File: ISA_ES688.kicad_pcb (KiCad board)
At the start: 4 copper layers, 104.1 x 99.1 mm, 114 parts, among them J1 ISA BUS, J2 Interrupt Select, J3 Address Select, J4 DMA Select, J5 Joystick/MIDI, J6 LINE OUT, J7 MIC, J8 LINE IN, J9 SPKR OUT, U1 74LS14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

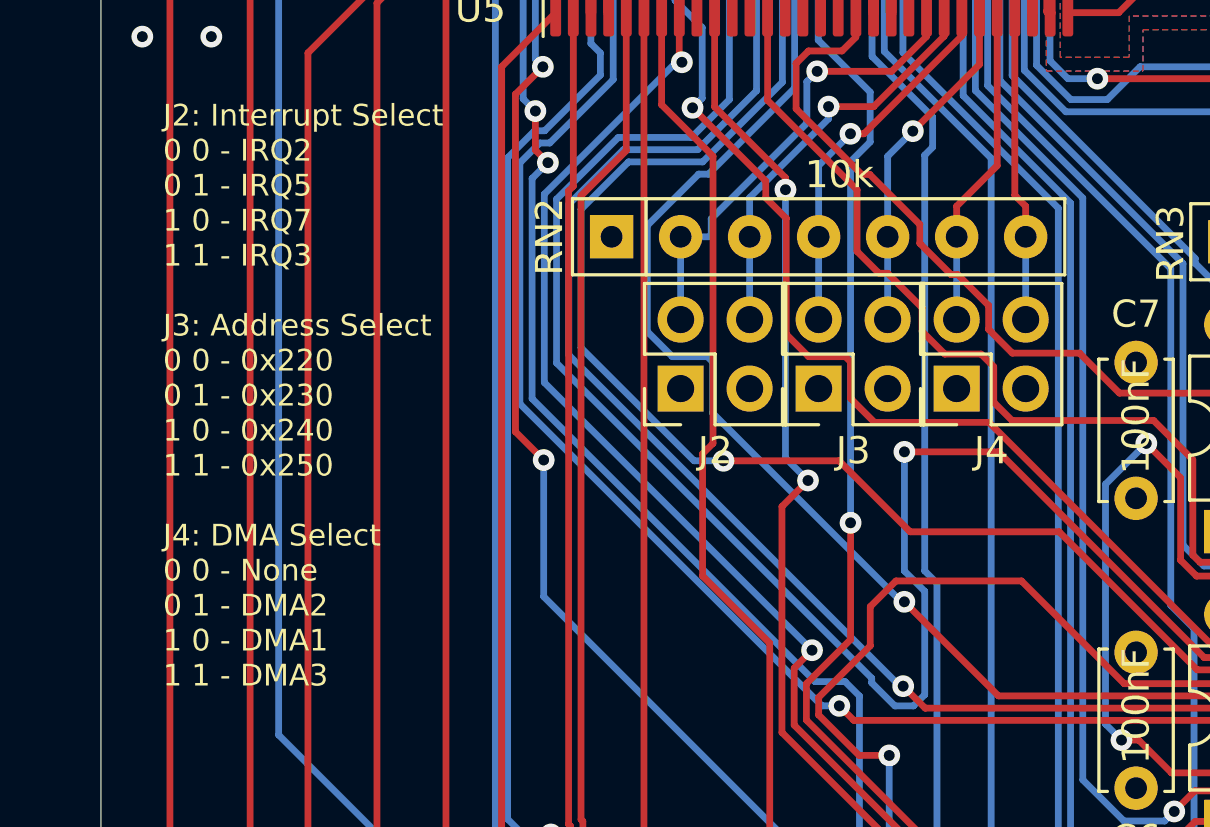
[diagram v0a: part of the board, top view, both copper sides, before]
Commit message: Updated silkscreen and version on schematic
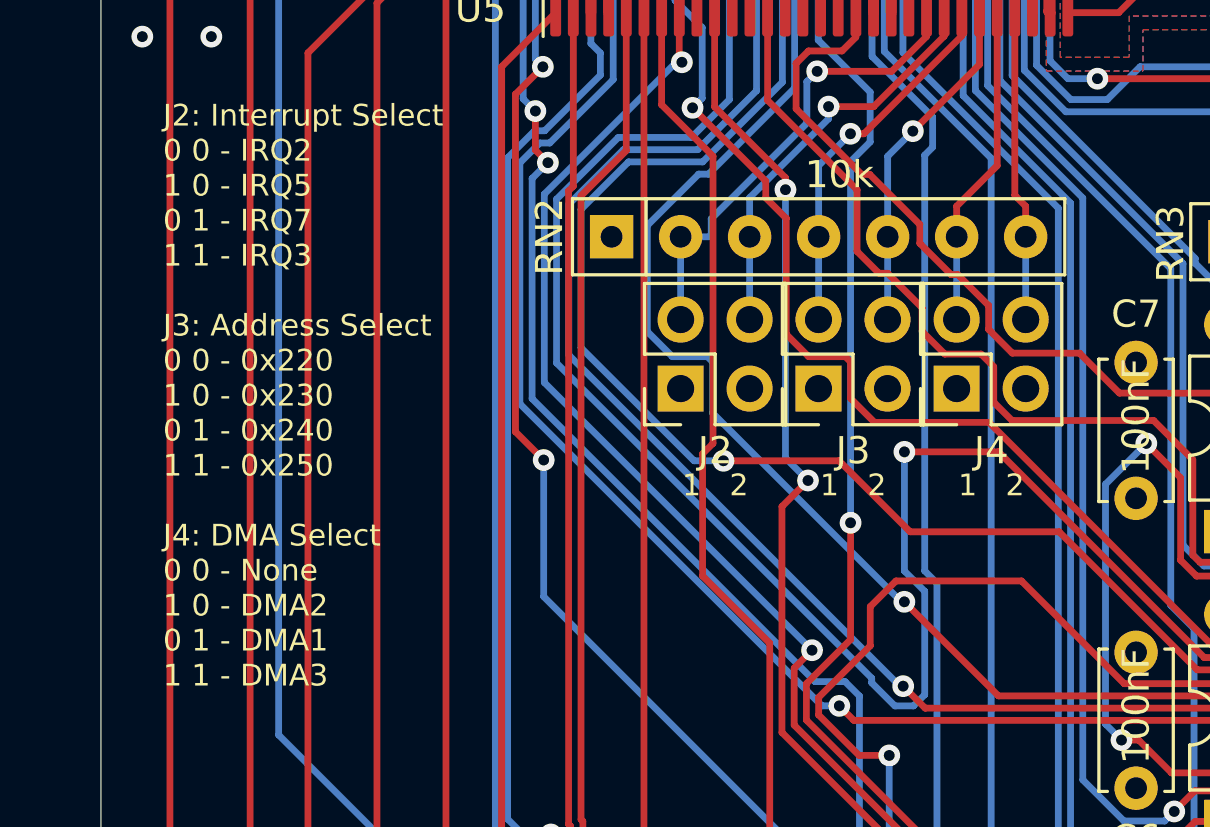
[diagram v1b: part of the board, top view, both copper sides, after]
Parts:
- R24, R25: value 220 -> DNM
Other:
- board text added: "1 2"
- board text added: "J2: Interrupt Select 0 0 - IRQ2 1 0 - IRQ5 0 1 - IRQ7 1 1 - IRQ3 J3: Address Select 0 0 - 0x220 1 0 - 0x230 0 1 - 0x240 1 1 - 0x250 J4: DMA Select 0 0 - None 1 0 - DMA2 0 1 - DMA1 1 1 - DMA3"
- board text removed: "J2: Interrupt Select 0 0 - IRQ2 0 1 - IRQ5 1 0 - IRQ7 1 1 - IRQ3 J3: Address Select 0 0 - 0x220 0 1 - 0x230 1 0 - 0x240 1 1 - 0x250 J4: DMA Select 0 0 - None 0 1 - DMA2 1 0 - DMA1 1 1 - DMA3"
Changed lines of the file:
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@@
   (general
     (thickness 1.6)
-    (drawings 25)
+    (drawings 28)
     (tracks 2205)
     (zones 0)
@@
     (add_net "Net-(C51-Pad2)")
     (add_net "Net-(C8-Pad2)")
+    (add_net "Net-(J1-Pad11)")
+    (add_net "Net-(J1-Pad12)")
+    (add_net "Net-(J1-Pad19)")
+    (add_net "Net-(J1-Pad20)")
+    (add_net "Net-(J1-Pad22)")
+    (add_net "Net-(J1-Pad24)")
+    (add_net "Net-(J1-Pad27)")
+    (add_net "Net-(J1-Pad28)")
+    (add_net "Net-(J1-Pad30)")
+    (add_net "Net-(J1-Pad32)")
+    (add_net "Net-(J1-Pad41)")
+    (add_net "Net-(J1-Pad43)")
+    (add_net "Net-(J1-Pad44)")
+    (add_net "Net-(J1-Pad45)")
+    (add_net "Net-(J1-Pad46)")
+    (add_net "Net-(J1-Pad47)")
+    (add_net "Net-(J1-Pad48)")
+    (add_net "Net-(J1-Pad49)")
+    (add_net "Net-(J1-Pad5)")
+    (add_net "Net-(J1-Pad50)")
+    (add_net "Net-(J1-Pad51)")
+    (add_net "Net-(J1-Pad52)")
+    (add_net "Net-(J1-Pad7)")
+    (add_net "Net-(J1-Pad8)")
     (add_net "Net-(J2-Pad2)")
     (add_net "Net-(J2-Pad4)")
@@
     (add_net "Net-(RN1-Pad4)")
     (add_net "Net-(RN1-Pad5)")
+    (add_net "Net-(U1-Pad10)")
+    (add_net "Net-(U1-Pad12)")
     (add_net "Net-(U1-Pad2)")
+    (add_net "Net-(U1-Pad4)")
+    (add_net "Net-(U1-Pad6)")
+    (add_net "Net-(U1-Pad8)")
+    (add_net "Net-(U5-Pad21)")
+    (add_net "Net-(U5-Pad34)")
+    (add_net "Net-(U5-Pad35)")
+    (add_net "Net-(U5-Pad49)")
+    (add_net "Net-(U5-Pad57)")
+    (add_net "Net-(U5-Pad72)")
+    (add_net "Net-(U5-Pad81)")
     (add_net "Net-(U7-Pad19)")
+    (add_net "Net-(U7-Pad2)")
     (add_net "Net-(U7-Pad20)")
     (add_net "Net-(U7-Pad21)")
+    (add_net "Net-(U7-Pad22)")
     (add_net "Net-(U7-Pad23)")
+    (add_net "Net-(U7-Pad9)")
+    (add_net "Net-(U8-Pad15)")
   )
   (net_class POWER ""
@@
       (effects (font (size 1 1) (thickness 0.15)) (justify mirror))
     )
-    (fp_text value 220 (at 0 1.778 90) (layer B.SilkS)
+    (fp_text value DNM (at 0 1.778 90) (layer B.SilkS)
       (effects (font (size 1 1) (thickness 0.15)) (justify mirror))
     )
@@
       (effects (font (size 1 1) (thickness 0.15)) (justify mirror))
     )
-    (fp_text value 220 (at 0 -1.82 90) (layer B.SilkS)
+    (fp_text value DNM (at 0 -1.82 90) (layer B.SilkS)
       (effects (font (size 1 1) (thickness 0.15)) (justify mirror))
     )
@@
   )
   (module Connector_PinHeader_2.54mm:PinHeader_2x02_P2.54mm_Vertical (layer F.Cu)
-    (at 237.236 171.196 90)
+    (at 237.231 171.196 90)
     (descr "Through hole straight pin header, 2x02, 2.54mm pitch, double rows")
     (tags "Through hole pin header THT 2x02 2.54mm double row")
@@
     )
   )
+  (gr_text "1   2" (at 243.591 174.752) (layer F.SilkS)
+    (effects (font (size 0.8 0.8) (thickness 0.2)))
+  )
+  (gr_text "1   2" (at 238.506 174.752) (layer F.SilkS)
+    (effects (font (size 0.8 0.8) (thickness 0.2)))
+  )
+  (gr_text "1   2" (at 233.431 174.752) (layer F.SilkS)
+    (effects (font (size 0.8 0.8) (thickness 0.2)))
+  )
   (gr_line (start 310.9468 115.3668) (end 360.6546 115.3668) (layer Dwgs.User) (width 0.15))
   (gr_line (start 307.34 126.7714) (end 360.7054 126.7714) (layer Dwgs.User) (width 0.15))
@@
     (effects (font (size 1.5 1.5) (thickness 0.3)))
   )
-  (gr_text "J2: Interrupt Select\n0 0 - IRQ2\n0 1 - IRQ5\n1 0 - IRQ7\n1 1 - IRQ3\n\nJ3: Address Select\n0 0 - 0x220\n0 1 - 0x230\n1 0 - 0x240\n1 1 - 0x250\n\nJ4: DMA Select\n0 0 - None\n0 1 - DMA2\n1 0 - DMA1\n1 1 - DMA3" (at 213.106 171.45) (layer F.SilkS)
+  (gr_text "J2: Interrupt Select\n0 0 - IRQ2\n1 0 - IRQ5\n0 1 - IRQ7\n1 1 - IRQ3\n\nJ3: Address Select\n0 0 - 0x220\n1 0 - 0x230\n0 1 - 0x240\n1 1 - 0x250\n\nJ4: DMA Select\n0 0 - None\n1 0 - DMA2\n0 1 - DMA1\n1 1 - DMA3" (at 213.106 171.45) (layer F.SilkS)
     (effects (font (size 0.8 0.8) (thickness 0.15)) (justify left))
   )

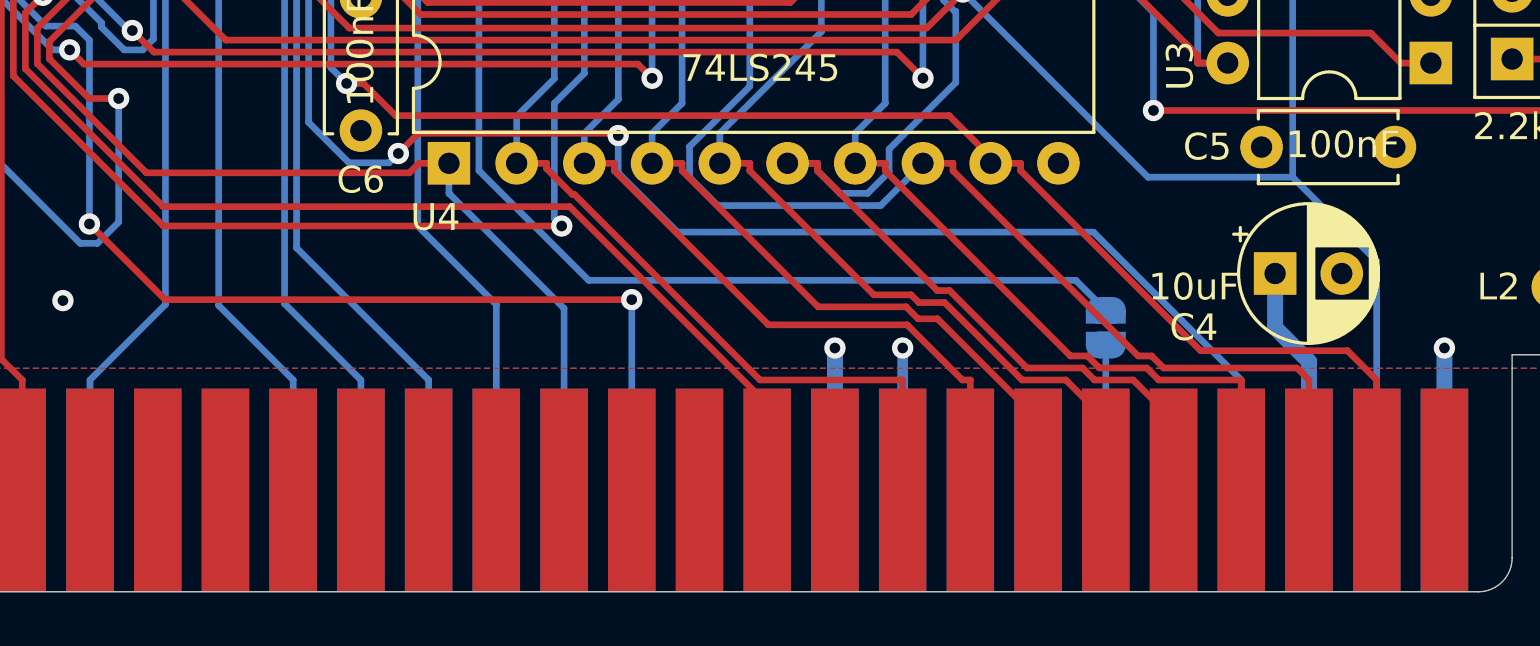
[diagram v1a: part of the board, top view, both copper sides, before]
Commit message: Reroute some traces
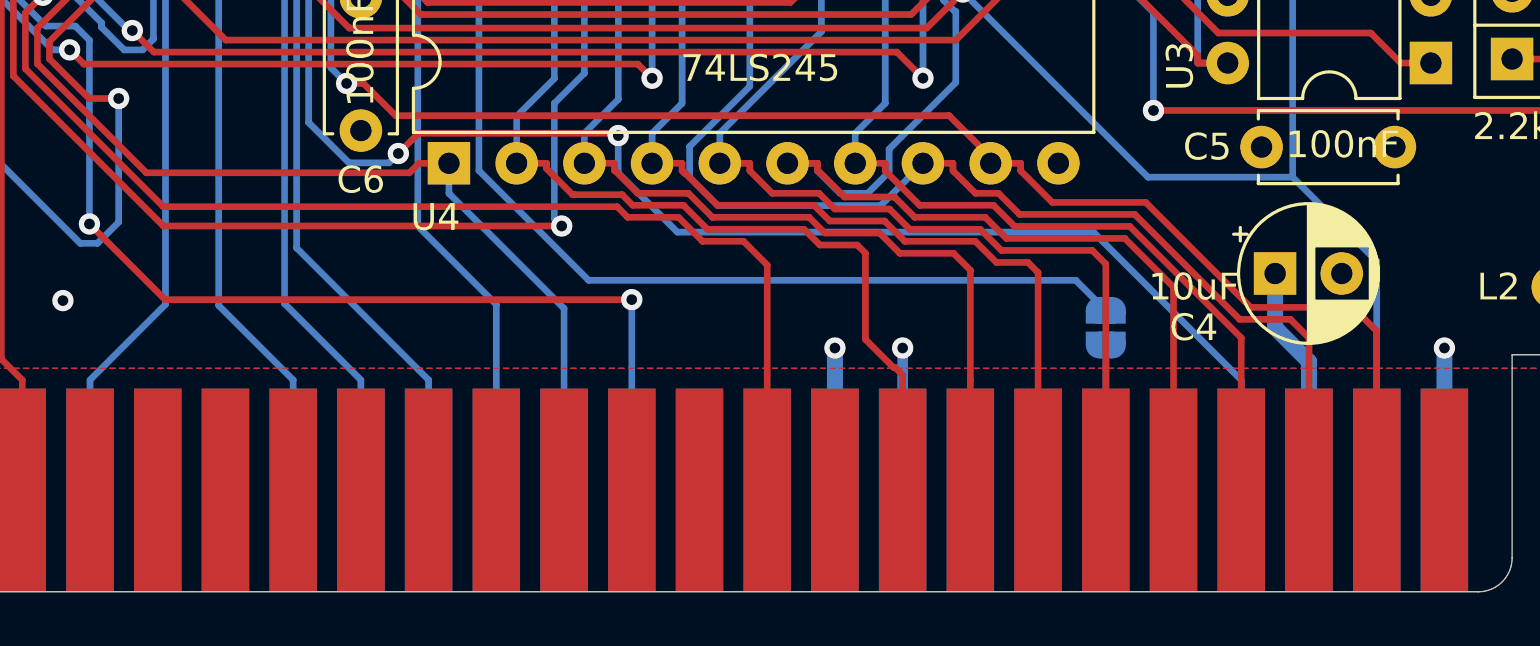
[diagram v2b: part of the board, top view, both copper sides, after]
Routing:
- net /AEN: track 69.1 -> 75.4 mm
- net /D3: track 43.9 -> 50.0 mm
- net /D2: track 42.9 -> 48.8 mm
- net /D4: track 39.0 -> 44.6 mm
- net /D1: track 51.5 -> 53.8 mm
- net /D0: track 41.4 -> 43.5 mm
- net /D7: track 72.0 -> 73.1 mm
- net /D6: track 44.6 -> 45.5 mm
- net /D5: track 33.7 -> 34.7 mm

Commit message: Change configuration pin description
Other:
- board text added: "220h"
- board text added: "230h"
- board text added: "240h"
- board text added: "250h"
- board text added: "DMA 1"
- board text added: "DMA 2"
- board text added: "DMA 3"
- board text added: "IRQ 2"
- board text added: "IRQ 3"
- board text added: "IRQ 5"
- board text added: "IRQ 7"
- board text added: "J2 IRQ"
- board text added: "J3 Addr."
- board text added: "J4 DMA"
- board text added: "None"
- board text removed: "1 2"
- board text removed: "J2: Interrupt Select 0 0 - IRQ2 1 0 - IRQ5 0 1 - IRQ7 1 1 - IRQ3 J3: Address Select 0 0 - 0x220 1 0 - 0x230 0 1 - 0x240 1 1 - 0x250 J4: DMA Select 0 0 - None 1 0 - DMA2 0 1 - DMA1 1 1 - DMA3"
